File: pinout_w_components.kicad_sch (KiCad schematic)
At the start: 28 parts, among them J1 10155435-00011LF, U10 ESDS304DBVR, U11 ESD351DPYR, U9 ESDS304DBVR

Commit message: update BOM
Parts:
- R21: value 22k1 -> 0; Part Number RC0201FR-0722K1L -> RC0402FR-070RL
- R22: value 3k3 -> 10M; Part Number RC0201FR-073K3L -> RC0201JR-0710ML; now not fitted
- R23: value 3k3 -> 0; Part Number RC0201FR-073K3L -> RC0402FR-070RL
- R24: now not fitted
- R29: value 1k2 -> 680; Part Number RC0402FR-071K5L -> RC0402FR-07680RL
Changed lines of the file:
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@@
 		(in_bom yes)
 		(on_board yes)
-		(dnp no)
+		(dnp yes)
 		(fields_autoplaced yes)
 		(property "Reference" "R22"
-			(at 121.92 149.86 0)
+			(at 121.92 149.8599 0)
 			(effects
 				(font
@@
 			)
 		)
-		(property "Value" "3k3"
-			(at 121.92 152.4 0)
+		(property "Value" "10M"
+			(at 121.92 152.3999 0)
 			(effects
 				(font
@@
 			)
 		)
-		(property "Part Number" "RC0201FR-073K3L"
+		(property "Part Number" "RC0201JR-0710ML"
 			(at 119.38 151.13 0)
 			(effects
@@
 			)
 		)
-		(property "Value" "22k1"
+		(property "Value" "0"
 			(at 121.92 142.24 0)
 			(effects
@@
 			)
 		)
-		(property "Part Number" "RC0201FR-0722K1L"
+		(property "Part Number" "RC0402FR-070RL"
 			(at 119.38 140.97 0)
 			(effects
@@
 		(in_bom yes)
 		(on_board yes)
-		(dnp no)
+		(dnp yes)
 		(fields_autoplaced yes)
 		(property "Reference" "R24"
@@
 		(fields_autoplaced yes)
 		(property "Reference" "R29"
-			(at 228.6 147.32 0)
+			(at 228.6 147.3199 0)
 			(effects
 				(font
@@
 			)
 		)
-		(property "Value" "1k2"
-			(at 228.6 149.86 0)
+		(property "Value" "680"
+			(at 228.6 149.8599 0)
 			(effects
 				(font
@@
 			)
 		)
-		(property "Part Number" "RC0402FR-071K5L"
+		(property "Part Number" "RC0402FR-07680RL"
 			(at 226.06 148.59 0)
 			(effects
@@
 		(fields_autoplaced yes)
 		(property "Reference" "R23"
-			(at 121.92 166.37 0)
+			(at 121.92 166.3699 0)
 			(effects
 				(font
@@
 			)
 		)
-		(property "Value" "3k3"
-			(at 121.92 168.91 0)
+		(property "Value" "0"
+			(at 121.92 168.9099 0)
 			(effects
 				(font
@@
 			)
 		)
-		(property "Part Number" "RC0201FR-073K3L"
+		(property "Part Number" "RC0402FR-070RL"
 			(at 119.38 167.64 0)
 			(effects

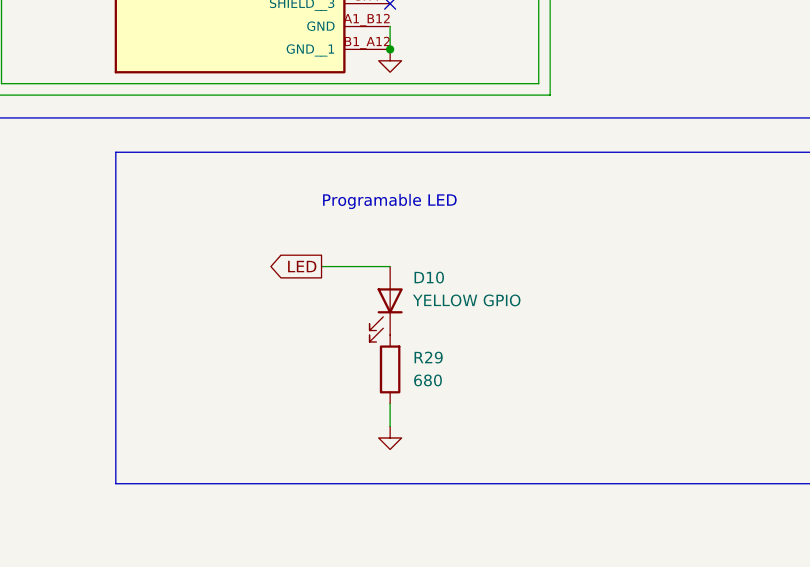
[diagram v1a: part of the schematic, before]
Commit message: change flash to sd flash, cleanup, and reconcile with F405FC
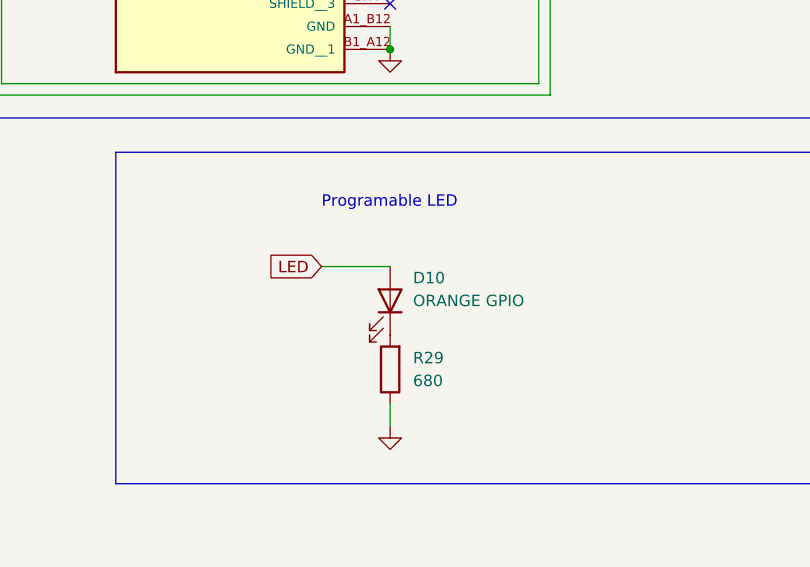
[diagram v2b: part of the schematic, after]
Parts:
- D10: value YELLOW GPIO -> ORANGE GPIO
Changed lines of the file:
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@@
 	)
 	(global_label "LED"
-		(shape output)
+		(shape input)
 		(at 218.44 137.16 180)
 		(fields_autoplaced yes)
@@
 			)
 		)
-		(property "Value" "YELLOW GPIO"
+		(property "Value" "ORANGE GPIO"
 			(at 228.6 140.97 90)
 			(effects
